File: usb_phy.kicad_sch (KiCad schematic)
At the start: 3 parts, among them J1 USB_C_Receptacle_USB2.0_14P, U1 USB3341

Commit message: develop: Did some stuff. Not sure what I am doing :).
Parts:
- removed J1: USB_C_Receptacle_USB2.0_14P, symbol Connector:USB_C_Receptacle_USB2.0_14P
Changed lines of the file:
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@@
-	)
-	(symbol
-		(lib_id "Connector:USB_C_Receptacle_USB2.0_14P")
-		(at 40.64 90.17 0)
-		(unit 1)
-		(exclude_from_sim no)
-		(in_bom yes)
-		(on_board yes)
-		(dnp no)
-		(fields_autoplaced yes)
-		(property "Reference" "J1"
-			(at 40.64 67.31 0)
-			(effects
-				(font
-					(size 1.27 1.27)
-				)
-			)
-		)
-		(property "Value" "USB_C_Receptacle_USB2.0_14P"
-			(at 40.64 69.85 0)
-			(effects
-				(font
-					(size 1.27 1.27)
-				)
-			)
-		)
-		(property "Footprint" ""
-			(at 44.45 90.17 0)
-			(effects
-				(font
-					(size 1.27 1.27)
-				)
-				(hide yes)
-			)
-		)
-		(property "Datasheet" "https://www.usb.org/sites/default/files/documents/usb_type-c.zip"
-			(at 44.45 90.17 0)
-			(effects
-				(font
-					(size 1.27 1.27)
-				)
-				(hide yes)
-			)
-		)
-		(property "Description" "USB 2.0-only 14P Type-C Receptacle connector"
-			(at 40.64 90.17 0)
-			(effects
-				(font
-					(size 1.27 1.27)
-				)
-				(hide yes)
-			)
-		)
-		(pin "B12"
-		)
-		(pin "A9"
-		)
-		(pin "B4"
-		)
-		(pin "S1"
-		)
-		(pin "A1"
-		)
-		(pin "B1"
-		)
-		(pin "A4"
-		)
-		(pin "A12"
-		)
-		(pin "B6"
-		)
-		(pin "B5"
-		)
-		(pin "B7"
-		)
-		(pin "A6"
-		)
-		(pin "A7"
-		)
-		(pin "A5"
-		)
-		(pin "B9"
-		)
-		(instances
-			(project ""
-				(path "/ba4aeeea-982a-4252-9638-c2cfeb24b844/dd519b02-51a3-46bd-88c4-26642ca77efc"
-					(reference "J1")
-					(unit 1)
-				)
-			)
-		)
 	)
 	(symbol

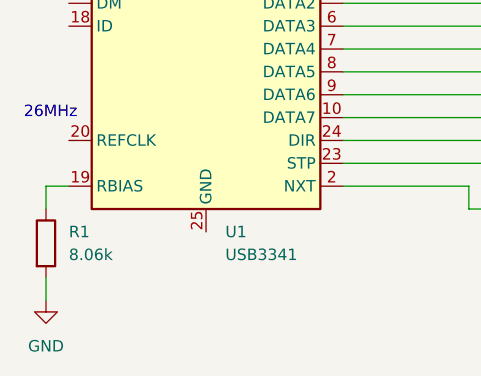
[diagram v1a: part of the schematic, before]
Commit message: develop: Added 1.8/3.3V and 0.95V power regulators.
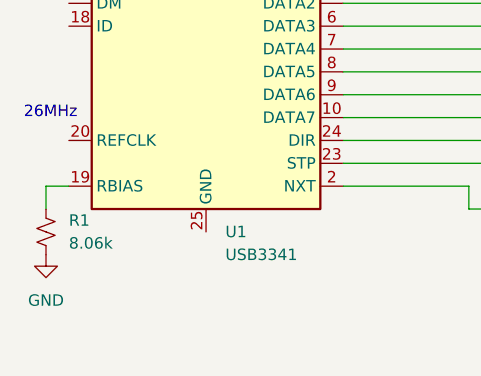
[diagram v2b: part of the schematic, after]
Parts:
- R1: symbol Device:R -> Device:R_Small_US
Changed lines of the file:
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@@
-		)
-	)
-	(wire
-		(pts
-			(xy 93.98 118.11) (xy 93.98 120.65)
-		)
-		(stroke
-			(width 0)
-			(type default)
 		)
 	)
@@
 	)
 	(symbol
-		(lib_id "Device:R")
-		(at 93.98 114.3 0)
+		(lib_id "Device:R_Small_US")
+		(at 93.98 113.03 0)
 		(unit 1)
 		(exclude_from_sim no)
@@
 		(fields_autoplaced yes)
 		(property "Reference" "R1"
-			(at 96.52 113.0299 0)
+			(at 96.52 111.7599 0)
 			(effects
 				(font
@@
 		)
 		(property "Value" "8.06k"
-			(at 96.52 115.5699 0)
+			(at 96.52 114.2999 0)
 			(effects
 				(font
@@
 		)
 		(property "Footprint" "Resistor_SMD:R_0402_1005Metric"
-			(at 92.202 114.3 90)
+			(at 93.98 113.03 0)
 			(effects
 				(font
@@
 		)
 		(property "Datasheet" "~"
-			(at 93.98 114.3 0)
-			(effects
-				(font
-					(size 1.27 1.27)
-				)
-				(hide yes)
-			)
-		)
-		(property "Description" "Resistor"
-			(at 93.98 114.3 0)
+			(at 93.98 113.03 0)
+			(effects
+				(font
+					(size 1.27 1.27)
+				)
+				(hide yes)
+			)
+		)
+		(property "Description" "Resistor, small US symbol"
+			(at 93.98 113.03 0)
 			(effects
 				(font
@@
 	(symbol
 		(lib_id "power:GND")
-		(at 93.98 120.65 0)
+		(at 93.98 115.57 0)
 		(unit 1)
 		(exclude_from_sim no)
@@
 		(fields_autoplaced yes)
 		(property "Reference" "#PWR01"
-			(at 93.98 127 0)
+			(at 93.98 121.92 0)
 			(effects
 				(font
@@
 		)
 		(property "Value" "GND"
-			(at 93.98 125.73 0)
+			(at 93.98 120.65 0)
 			(effects
 				(font
@@
 		)
 		(property "Footprint" ""
-			(at 93.98 120.65 0)
+			(at 93.98 115.57 0)
 			(effects
 				(font
@@
 		)
 		(property "Datasheet" ""
-			(at 93.98 120.65 0)
+			(at 93.98 115.57 0)
 			(effects
 				(font
@@
 		)
 		(property "Description" "Power symbol creates a global label with name \"GND\" , ground"
-			(at 93.98 120.65 0)
-			(effects
-				(font
+			(at 93.98 115.57 0)
+			(effects
+				(font
